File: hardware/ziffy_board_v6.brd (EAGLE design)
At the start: 52 x 50 mm, 27 parts, among them IC1 74HC125, IC2 74HC125, IC3 74HC125, IC4 74HC125, IC5 74HC125, IC6 74HC125

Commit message: tweaked
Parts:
- C1, C2: value 1uF -> 0.1uF; device A_butts:C025-024X044 -> A_butts:C0603
- C3, C4, C5, C6: device A_butts:C025-024X044 -> A_butts:C0603
- C7: value 0.1uF -> 1uF
- C8: value 0.1uF -> 1uF; device A_butts:C025-024X044 -> A_butts:C0805
- R4: device A_butts:RESISTOR-AXIAL-PTH-6.35MM -> A_butts:RESISTOR-AXIAL-PTH-5.08MM
- moved C5 48.1 mm to (44.0, 10.5), flipped to the bottom, turned to 0 degrees
- moved C7 43.5 mm to (47.8, 24.2), turned to 90 degrees
- moved C6 43.0 mm to (47.5, 30.0), flipped to the bottom, turned to 90 degrees
- moved C8 35.9 mm to (1.65, 6.82)
- moved C4 34.6 mm to (17.5, 14.9), flipped to the bottom, turned to 90 degrees
- moved C2 33.8 mm to (17.3, 45.0), flipped to the bottom, turned to 90 degrees
- moved IC5 30.2 mm to (41.0, 15.0), turned to 180 degrees
- moved C1 20.5 mm to (47.5, 45.0), flipped to the bottom
- moved BUSY 20.4 mm to (66.5, 49.8)
- moved ERR 20.4 mm to (62.0, 49.8)
- moved HI! 20.4 mm to (57.5, 49.8)
- moved R1 20.4 mm to (67.5, 42.8)
- moved R2 20.4 mm to (65.0, 42.8)
- moved R3 20.4 mm to (62.5, 42.8)
- moved C3 17.6 mm to (17.4, 30.0), flipped to the bottom, turned to 90 degrees
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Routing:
- net P_ATTINY2313: track 81.5 -> 28.1 mm, vias 6 -> 1
- net Z25: track 29.9 -> 0.00 mm
- net P_ATTINY85: track 52.9 -> 24.2 mm, vias 6 -> 1
- net SCK: track 22.2 -> 48.4 mm
- net VCC: track 50.3 -> 24.9 mm, vias 0 -> 1
- net MISO: track 41.3 -> 20.7 mm, vias 3 -> 0
- net Z4: track 19.1 -> 0.00 mm, vias 2 -> 0
- net Z1: track 21.5 -> 5.30 mm, vias 2 -> 0
- net TAR_RST: track 71.8 -> 85.0 mm, vias 1 -> 3
- net P_ATTINY84: track 46.2 -> 37.9 mm, vias 6 -> 2
- net MOSI: track 34.1 -> 26.2 mm, vias 2 -> 1
- net Z18: track 7.42 -> 0.00 mm
- net Z27: track 6.65 -> 0.00 mm, vias 2 -> 0
- net Z7: track 2.79 -> 0.00 mm, vias 1 -> 0
- net P_ATMEGA328P: track 40.8 -> 42.5 mm, vias 4 -> 2
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- added copper zone on layer 16, net GND

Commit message: more twaddling
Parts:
- BUSY, ERR, HI!: device A_butts:LED3MM -> A_butts:LED-1206
- R1, R2, R3: device A_butts:RESISTOR-AXIAL-PTH-6.35MM -> A_butts:R0805
- moved C1 31.0 mm to (16.5, 45.5), flipped to the top
- moved IC1 31.0 mm to (10.0, 45.5)
- moved R1 27.5 mm to (40.5, 48.0), turned to 180 degrees
- moved R2 24.6 mm to (40.5, 45.5), turned to 180 degrees
- moved R3 22.0 mm to (40.5, 43.0), turned to 180 degrees
- moved BUSY 21.1 mm to (45.5, 48.0), turned to 180 degrees
- moved ERR 17.1 mm to (45.5, 45.5), turned to 180 degrees
- moved HI! 13.8 mm to (45.5, 43.0), turned to 180 degrees
- moved IC5 10.5 mm to (41.0, 25.5)
- moved C2 9.55 mm to (16.3, 35.5), flipped to the top
- moved IC2 9.55 mm to (10.0, 35.5)
- moved C5 9.53 mm to (44.8, 20.0), flipped to the top, turned to 270 degrees
- moved C6 5.50 mm to (47.5, 35.5), flipped to the top
- moved IC6 5.50 mm to (41.0, 35.5)
- moved C3 4.61 mm to (16.4, 25.5), flipped to the top
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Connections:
- net GND: now also R1.2, R2.2, R3.2; no longer R1.P$2, R2.P$2, R3.P$2
- net N$1: now also BUSY.C, R1.1; no longer BUSY.K, R1.P$1
- net N$2: now also ERR.C, R2.1; no longer ERR.K, R2.P$1
- net N$3: now also HI!.C, R3.1; no longer HI!.K, R3.P$1
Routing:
- net VCC: track 24.9 -> 112.5 mm, vias 1 -> 5
- net P_ATTINY85: track 24.2 -> 70.3 mm, vias 1 -> 6
- net Z20: track 0.00 -> 45.8 mm, vias 0 -> 1
- net P_ATTINY2313: track 28.1 -> 72.2 mm, vias 1 -> 6
- net Z26: track 0.00 -> 42.1 mm, vias 0 -> 1
- net Z25: track 0.00 -> 32.6 mm
- net Z22: track 0.00 -> 32.4 mm, vias 0 -> 2
- net Z17: track 0.00 -> 30.8 mm, vias 0 -> 3
- net Z28: track 0.00 -> 29.2 mm, vias 0 -> 2
- net Z1: track 5.30 -> 30.3 mm, vias 0 -> 2
- net P_ATMEGA328P: track 42.5 -> 64.5 mm, vias 2 -> 6
- net Z18: track 0.00 -> 21.9 mm
- net Z7: track 0.00 -> 20.7 mm
- net Z4: track 0.00 -> 19.4 mm
- net SCK: track 48.4 -> 67.3 mm
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
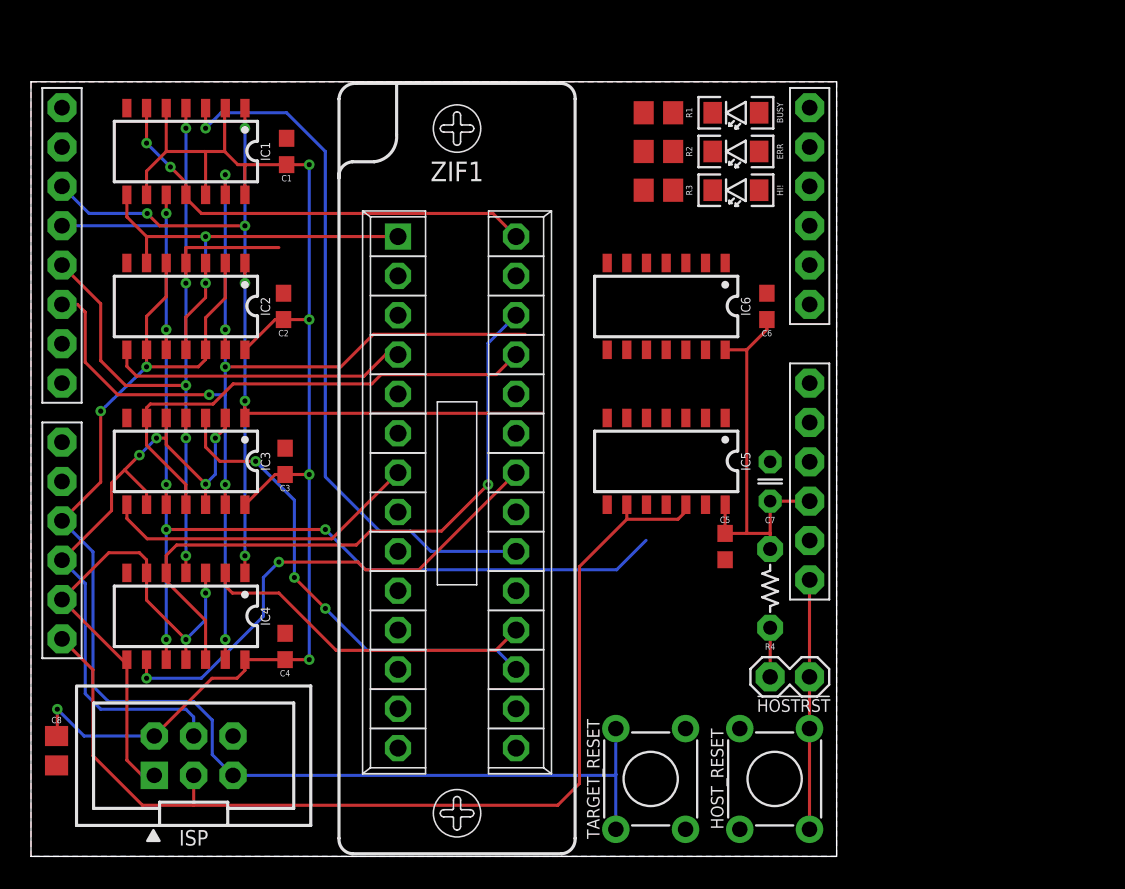
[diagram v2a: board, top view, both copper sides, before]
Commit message: routing done! mostly. now trying to return to pin-compat with original code base
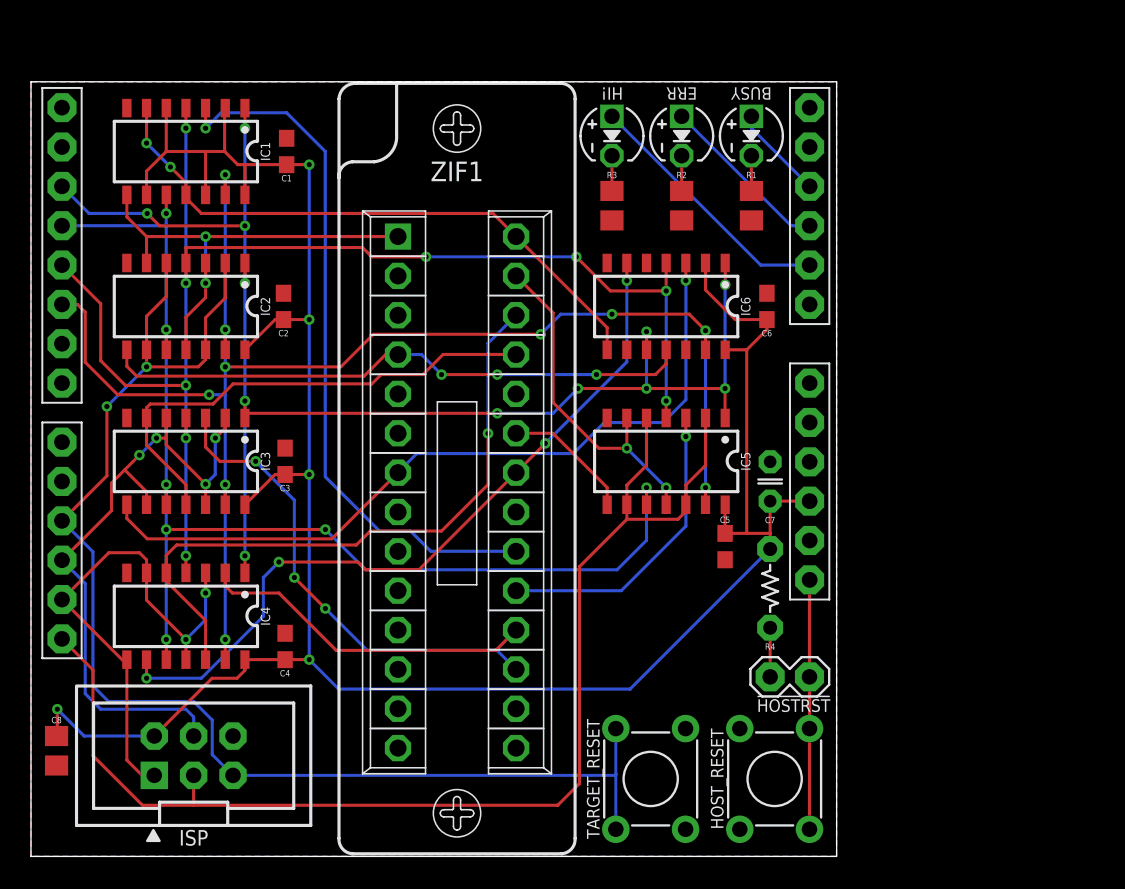
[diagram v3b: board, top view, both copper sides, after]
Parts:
- BUSY, ERR, HI!: device A_butts:LED-1206 -> A_butts:LED3MM
- moved HI! 8.73 mm to (37.5, 46.5), turned to 270 degrees
- moved R1 8.49 mm to (46.5, 42.0), turned to 270 degrees
- moved R2 3.81 mm to (42.0, 42.0), turned to 270 degrees
- moved ERR 3.64 mm to (42.0, 46.5), turned to 270 degrees
- moved R3 3.16 mm to (37.5, 42.0), turned to 270 degrees
- moved BUSY 1.80 mm to (46.5, 46.5), turned to 270 degrees
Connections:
- net BUSY: now also SHIELD.D9
- net ERROR: now also SHIELD.D8
- net HELLO: now also SHIELD.D7
- net N$1: now also BUSY.K; no longer BUSY.C
- net N$2: now also ERR.K; no longer ERR.C
- net N$3: now also HI!.K; no longer HI!.C
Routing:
- net VCC: track 112.5 -> 153.3 mm
- net P_ATTINY84: track 53.0 -> 89.1 mm, vias 5 -> 9
- net Z7: track 20.7 -> 50.1 mm, vias 0 -> 1
- net P_ATMEGA328P: track 64.5 -> 91.8 mm, vias 6 -> 12
- net P_ATTINY85: track 70.3 -> 95.4 mm, vias 6 -> 10
- net Z27: track 0.00 -> 21.8 mm, vias 0 -> 2
- net Z19: track 0.00 -> 19.7 mm, vias 0 -> 1
- net Z4: track 19.4 -> 38.4 mm, vias 0 -> 3
- net HELLO: track 0.00 -> 16.7 mm
- net Z22: track 32.4 -> 48.9 mm, vias 2 -> 4
- net SCK: track 67.3 -> 79.6 mm
- net ERROR: track 0.00 -> 11.2 mm
- net Z28: track 29.2 -> 38.9 mm
- net Z23: track 0.00 -> 8.44 mm
- net BUSY: track 0.00 -> 6.08 mm
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
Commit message: more trying to return to pin-compat with original code base
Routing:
- net BUSY: track 6.08 -> 73.9 mm, vias 0 -> 1
- net ERROR: track 11.2 -> 70.5 mm, vias 0 -> 1
- net HELLO: track 16.7 -> 67.3 mm
- net P_ATMEGA328P: track 91.8 -> 93.3 mm, vias 12 -> 13
- net Z20: track 45.8 -> 45.0 mm
- net MOSI: track 43.4 -> 42.9 mm
- net P_ATTINY2313: vias 7 -> 8
- net TAR_RST: vias 2 -> 1
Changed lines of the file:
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@@
 <via x="8.1" y="27" extent="1-16" drill="0.3302"/>
 <wire x1="8.1" y1="27" x2="8.73" y2="27" width="0.2" layer="1"/>
-<wire x1="5.2" y1="22.32" x2="5.2" y2="24.1" width="0.2" layer="1"/>
-<wire x1="5.2" y1="24.1" x2="6.05" y2="24.95" width="0.2" layer="1"/>
-<via x="7" y="25.9" extent="1-16" drill="0.3302"/>
-<wire x1="6.05" y1="24.95" x2="7" y2="25.9" width="0.2" layer="1"/>
-<wire x1="7" y1="25.9" x2="8.1" y2="27" width="0.2" layer="16"/>
-<wire x1="7.46" y1="22.7" x2="7.46" y2="23.54" width="0.2" layer="1"/>
-<wire x1="7.46" y1="23.54" x2="6.05" y2="24.95" width="0.2" layer="1"/>
+<via x="7.46" y="24" extent="1-16" drill="0.3302"/>
+<wire x1="7.46" y1="24" x2="7.46" y2="26.36" width="0.2" layer="16"/>
+<wire x1="7.46" y1="26.36" x2="8.1" y2="27" width="0.2" layer="16"/>
+<wire x1="5.2" y1="22.32" x2="5.2" y2="23.5" width="0.2" layer="1"/>
+<wire x1="5.2" y1="23.5" x2="5.7" y2="24" width="0.2" layer="1"/>
+<wire x1="5.7" y1="24" x2="7.46" y2="24" width="0.2" layer="1"/>
+<wire x1="7.46" y1="24" x2="7.46" y2="22.7" width="0.2" layer="1"/>
 </signal>
 <signal name="SCK">
@@
 <wire x1="13.04" y1="5.23" x2="11.7" y2="6.57" width="0.2" layer="16"/>
 <wire x1="11.7" y1="6.57" x2="11.7" y2="8.8" width="0.2" layer="16"/>
-<wire x1="2" y1="21.66" x2="4.9" y2="24.56" width="0.2" layer="1"/>
-<wire x1="4.9" y1="24.56" x2="4.9" y2="29.04" width="0.2" layer="1"/>
 <wire x1="11.27" y1="34.77" x2="12.54" y2="36.04" width="0.2" layer="1"/>
 <wire x1="12.54" y1="36.04" x2="12.54" y2="38.3" width="0.2" layer="1"/>
@@
 <wire x1="7.46" y1="32.7" x2="7.46" y2="31.6" width="0.2" layer="1"/>
 <via x="7.46" y="31.6" extent="1-16" drill="0.3302"/>
-<wire x1="7.46" y1="31.6" x2="4.9" y2="29.04" width="0.2" layer="16"/>
-<via x="4.9" y="29.04" extent="1-16" drill="0.3302"/>
 <wire x1="11.27" y1="32.7" x2="11.27" y2="34.77" width="0.2" layer="1"/>
+<wire x1="2" y1="21.66" x2="7.46" y2="27.12" width="0.2" layer="16"/>
+<wire x1="7.46" y1="27.12" x2="7.46" y2="31.6" width="0.2" layer="16"/>
 </signal>
 <signal name="HELLO">
@@
 <wire x1="47.1" y1="38.17" x2="50.26" y2="38.17" width="0.2" layer="16"/>
 <contactref element="SHIELD" pad="D7"/>
-<wire x1="2" y1="30.55" x2="37.5" y2="47.77" width="0" layer="19" extent="1-1"/>
+<wire x1="2" y1="30.55" x2="3.5" y2="32.05" width="0.2" layer="16"/>
+<wire x1="3.5" y1="32.05" x2="3.5" y2="44.7" width="0.2" layer="16"/>
+<wire x1="3.5" y1="44.7" x2="7.2" y2="48.4" width="0.2" layer="16"/>
+<wire x1="7.2" y1="48.4" x2="36.87" y2="48.4" width="0.2" layer="16"/>
+<wire x1="36.87" y1="48.4" x2="37.5" y2="47.77" width="0.2" layer="16"/>
 </signal>
 <signal name="ERROR">
@@
 <wire x1="49.06" y1="40.71" x2="50.26" y2="40.71" width="0.2" layer="16"/>
 <contactref element="SHIELD" pad="D8"/>
-<wire x1="2" y1="26.74" x2="42" y2="47.77" width="0" layer="19" extent="1-1"/>
+<wire x1="2" y1="26.74" x2="3.9" y2="28.64" width="0.2" layer="16"/>
+<wire x1="3.9" y1="28.64" x2="3.9" y2="44.6" width="0.2" layer="16"/>
+<wire x1="3.9" y1="44.6" x2="7.3" y2="48" width="0.2" layer="16"/>
+<wire x1="7.3" y1="48" x2="34.5" y2="48" width="0.2" layer="16"/>
+<wire x1="34.5" y1="48" x2="36" y2="46.5" width="0.2" layer="16"/>
+<via x="36" y="46.5" extent="1-16" drill="0.3302"/>
+<wire x1="36" y1="46.5" x2="40.73" y2="46.5" width="0.2" layer="1"/>
+<wire x1="40.73" y1="46.5" x2="42" y2="47.77" width="0.2" layer="1"/>
 </signal>
 <signal name="BUSY">
@@
 <wire x1="46.5" y1="47.01" x2="46.5" y2="47.77" width="0.2" layer="16"/>
 <contactref element="SHIELD" pad="D9"/>
-<wire x1="2" y1="24.2" x2="46.5" y2="47.01" width="0" layer="19" extent="16-16"/>
+<wire x1="2" y1="24.2" x2="4.3" y2="26.5" width="0.2" layer="16"/>
+<wire x1="4.3" y1="26.5" x2="4.3" y2="44.5" width="0.2" layer="16"/>
+<wire x1="4.3" y1="44.5" x2="7.4" y2="47.6" width="0.2" layer="16"/>
+<wire x1="7.4" y1="47.6" x2="32.9" y2="47.6" width="0.2" layer="16"/>
+<wire x1="32.9" y1="47.6" x2="36.5" y2="44" width="0.2" layer="16"/>
+<wire x1="36.5" y1="44" x2="39" y2="44" width="0.2" layer="16"/>
+<via x="39" y="44" extent="1-16" drill="0.3302"/>
+<wire x1="39" y1="44" x2="41.5" y2="46.5" width="0.2" layer="1"/>
+<wire x1="41.5" y1="46.5" x2="45.23" y2="46.5" width="0.2" layer="1"/>
+<wire x1="45.23" y1="46.5" x2="46.5" y2="47.77" width="0.2" layer="1"/>
 </signal>
 <signal name="VCC">
@@
 <wire x1="11.27" y1="48.3" x2="11.27" y2="47" width="0.2" layer="1"/>
 <via x="11.27" y="47" extent="1-16" drill="0.3302"/>
-<wire x1="11.27" y1="47" x2="12.27" y2="48" width="0.2" layer="16"/>
-<wire x1="12.27" y1="48" x2="16.5" y2="48" width="0.2" layer="16"/>
+<wire x1="11.27" y1="47" x2="17.5" y2="47" width="0.2" layer="16"/>
 <wire x1="31.31" y1="19.69" x2="25.81" y2="19.69" width="0.2" layer="16"/>
 <wire x1="25.81" y1="19.69" x2="24.5" y2="21" width="0.2" layer="16"/>
@@
 <wire x1="22.5" y1="21" x2="19" y2="24.5" width="0.2" layer="16"/>
 <wire x1="19" y1="24.5" x2="19" y2="45.5" width="0.2" layer="16"/>
-<wire x1="19" y1="45.5" x2="16.5" y2="48" width="0.2" layer="16"/>
+<wire x1="19" y1="45.5" x2="17.5" y2="47" width="0.2" layer="16"/>
 </signal>
 <signal name="Z19">
@@
 <wire x1="13.81" y1="28.6" x2="13.81" y2="29.4" width="0.2" layer="1"/>
 <wire x1="13.81" y1="38.3" x2="13.81" y2="37" width="0.2" layer="1"/>
-<wire x1="13.81" y1="48.3" x2="13.81" y2="47" width="0.2" layer="1"/>
-<via x="13.81" y="47" extent="1-16" drill="0.3302"/>
-<wire x1="13.81" y1="47" x2="13.81" y2="40.7" width="0.2" layer="16"/>
+<wire x1="13.81" y1="48.3" x2="13.81" y2="45.5" width="0.2" layer="1"/>
+<via x="13.81" y="45.5" extent="1-16" drill="0.3302"/>
+<wire x1="13.81" y1="45.5" x2="13.81" y2="40.7" width="0.2" layer="16"/>
 <via x="13.81" y="37" extent="1-16" drill="0.3302"/>
 <wire x1="13.81" y1="40.7" x2="13.81" y2="37" width="0.2" layer="16"/>
-<wire x1="2" y1="43.25" x2="3.75" y2="41.5" width="0.2" layer="16"/>
-<wire x1="3.75" y1="41.5" x2="7.5" y2="41.5" width="0.2" layer="16"/>
 <via x="7.5" y="41.5" extent="1-16" drill="0.3302"/>
 <wire x1="7.5" y1="41.5" x2="8.3" y2="40.7" width="0.2" layer="1"/>
@@
 <wire x1="44.8" y1="36.89" x2="44.81" y2="36.9" width="0.2" layer="16"/>
 <wire x1="44.81" y1="36.9" x2="44.81" y2="38.3" width="0.2" layer="1"/>
+<via x="6.5" y="44" extent="1-16" drill="0.3302"/>
+<wire x1="6.5" y1="44" x2="7.5" y2="43" width="0.2" layer="16"/>
+<wire x1="7.5" y1="43" x2="7.5" y2="41.5" width="0.2" layer="16"/>
+<wire x1="2" y1="43.25" x2="2.75" y2="44" width="0.2" layer="1"/>
+<wire x1="2.75" y1="44" x2="6.5" y2="44" width="0.2" layer="1"/>
 </signal>
 <signal name="P_ATTINY2313">
@@
 <wire x1="8.73" y1="42.7" x2="8.73" y2="41.5" width="0.2" layer="1"/>
 <via x="8.73" y="34" extent="1-16" drill="0.3302"/>
-<wire x1="8.73" y1="34" x2="8.73" y2="40.8" width="0.2" layer="16"/>
-<wire x1="8.73" y1="40.8" x2="8.73" y2="41.5" width="0.2" layer="16"/>
+<wire x1="8.73" y1="34" x2="8.73" y2="40.6" width="0.2" layer="16"/>
 <via x="8.73" y="41.5" extent="1-16" drill="0.3302"/>
-<wire x1="2" y1="40.71" x2="8.64" y2="40.71" width="0.2" layer="16"/>
-<wire x1="8.64" y1="40.71" x2="8.73" y2="40.8" width="0.2" layer="16"/>
 <via x="8.73" y="24" extent="1-16" drill="0.3302"/>
+<wire x1="8.73" y1="40.71" x2="8.73" y2="41.5" width="0.2" layer="16"/>
 <wire x1="8.73" y1="24" x2="8.73" y2="34" width="0.2" layer="16"/>
 <via x="8.73" y="14" extent="1-16" drill="0.3302"/>
@@
 <via x="39.73" y="23.8" extent="1-16" drill="0.3302"/>
 <wire x1="39.73" y1="23.8" x2="39.73" y2="22.7" width="0.2" layer="1"/>
+<wire x1="2" y1="40.71" x2="5.5" y2="40.71" width="0.2" layer="1"/>
+<via x="5.5" y="40.71" extent="1-16" drill="0.3302"/>
+<wire x1="5.5" y1="40.71" x2="8.73" y2="40.71" width="0.2" layer="16"/>
+<wire x1="8.73" y1="40.71" x2="8.73" y2="40.6" width="0.2" layer="16"/>
 </signal>
 <signal name="P_ATTINY84">

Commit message: layout complete. replaced most of the surface mount caps w/PTH ones. still debating resistors for LEDs.
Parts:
- removed C8: 1uF, A_butts:C0805
- added U$1: (no value), A_butts:CC-BY-SA-4.0-NO-URL
- added U$2: (no value), A_butts:OSHWLOGO_TOP_0.2_A
- C1, C2, C3, C4, C6: device A_butts:C0603 -> A_butts:C025-024X044
- C5: value 0.1uF -> 1uF; device A_butts:C0603 -> A_butts:C025-024X044
- SHIELD: value (none) -> YOUR MOTHER
- moved C7 49.3 mm to (1.65, 6.50), turned to 270 degrees
- moved C5 4.74 mm to (47.0, 24.2), turned to 90 degrees
- moved C1 1.33 mm to (16.0, 44.3)
- moved R4 0.77 mm to (47.0, 17.0)
- moved C4 0.58 mm to (16.0, 14.0)
- moved C6 0.50 mm to (47.0, 35.5)
- moved C3 0.40 mm to (16.0, 25.5)
- moved C2 0.30 mm to (16.0, 35.5)
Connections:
- net BUSY: no longer SHIELD.A3
- net ERROR: no longer SHIELD.A2
- net GND: no longer C8.2
- net HELLO: no longer SHIELD.A1
- net VCC: no longer C8.1
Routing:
- net HELLO: track 67.3 -> 50.6 mm
- net ERROR: track 70.5 -> 59.3 mm, vias 1 -> 0
- net VCC: track 153.3 -> 144.5 mm, vias 5 -> 0
- net BUSY: track 73.9 -> 67.8 mm, vias 1 -> 0
- net MISO: track 33.8 -> 29.5 mm
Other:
- outline, holes or cut-outs redrawn
- board text added: "AVR ZIFFY"
- board text added: "Revision 6.0"
- board text added: "by schizobovine <sean@yak.net>"
